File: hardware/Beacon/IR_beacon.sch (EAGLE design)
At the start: 10 parts

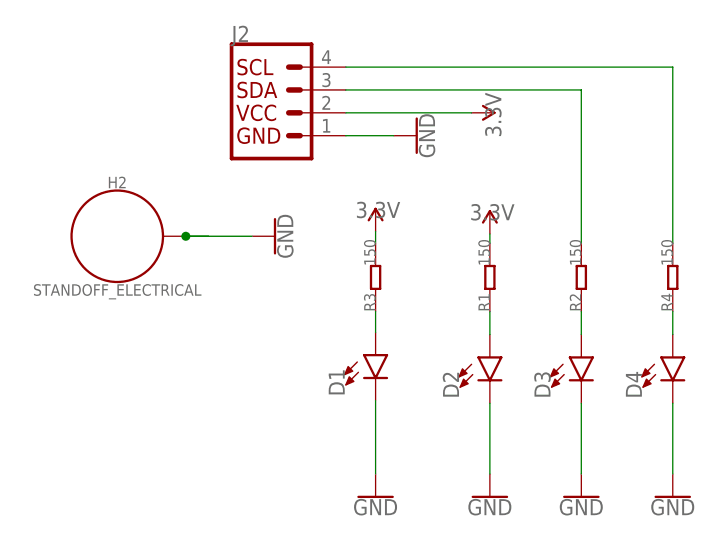
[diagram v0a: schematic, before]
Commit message: Finished Cad files for beacon, and added new 5 bit patern for markers.
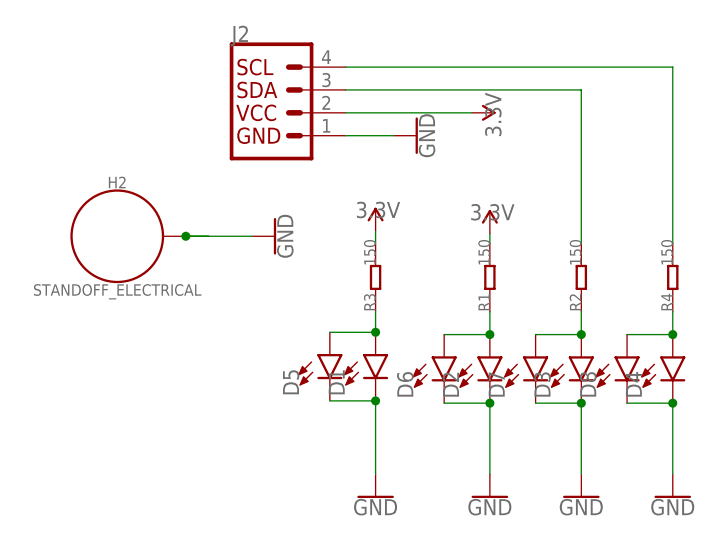
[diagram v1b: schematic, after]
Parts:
- added D5, D6, D7, D8: (no value), SparkFun-LED:LED-FKIT-1206
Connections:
- net GND: now also D5.C, D6.C, D7.C, D8.C
- net N$2: now also D5.A
- net N$3: now also D7.A
- net N$4: now also D6.A
- net N$5: now also D8.A
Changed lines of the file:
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@@
 <?xml version="1.0" encoding="utf-8"?>
 <!DOCTYPE eagle SYSTEM "eagle.dtd">
-<eagle version="9.2.2">
+<eagle version="9.4.2">
 <drawing>
 <settings>
@@
 <part name="J2" library="IAD-Library" deviceset="QWIIC_CONNECTOR" device="JS-1MM"/>
 <part name="H2" library="IAD-Library" deviceset="STANDOFF_ELECTRICAL" device=""/>
+<part name="D5" library="SparkFun-LED" deviceset="LED" device="-FKIT-1206"/>
+<part name="D6" library="SparkFun-LED" deviceset="LED" device="-FKIT-1206"/>
+<part name="D7" library="SparkFun-LED" deviceset="LED" device="-FKIT-1206"/>
+<part name="D8" library="SparkFun-LED" deviceset="LED" device="-FKIT-1206"/>
 </parts>
 <sheets>
@@
 <attribute name="VALUE" x="149.86" y="65.786" size="1.27" layer="96" font="vector" rot="R180" align="bottom-center"/>
 </instance>
+<instance part="D5" gate="G$1" x="173.482" y="57.912" smashed="yes">
+<attribute name="NAME" x="170.053" y="53.34" size="1.778" layer="95" font="vector" rot="R90"/>
+<attribute name="VALUE" x="175.387" y="53.34" size="1.778" layer="96" font="vector" rot="R90" align="top-left"/>
+</instance>
+<instance part="D6" gate="G$1" x="186.182" y="57.658" smashed="yes">
+<attribute name="NAME" x="182.753" y="53.086" size="1.778" layer="95" font="vector" rot="R90"/>
+<attribute name="VALUE" x="188.087" y="53.086" size="1.778" layer="96" font="vector" rot="R90" align="top-left"/>
+</instance>
+<instance part="D7" gate="G$1" x="196.342" y="57.658" smashed="yes">
+<attribute name="NAME" x="192.913" y="53.086" size="1.778" layer="95" font="vector" rot="R90"/>
+<attribute name="VALUE" x="198.247" y="53.086" size="1.778" layer="96" font="vector" rot="R90" align="top-left"/>
+</instance>
+<instance part="D8" gate="G$1" x="206.502" y="57.658" smashed="yes">
+<attribute name="NAME" x="203.073" y="53.086" size="1.778" layer="95" font="vector" rot="R90"/>
+<attribute name="VALUE" x="208.407" y="53.086" size="1.778" layer="96" font="vector" rot="R90" align="top-left"/>
+</instance>
 </instances>
 <busses>
@@
 <wire x1="178.562" y1="62.738" x2="178.562" y2="60.452" width="0.1524" layer="91"/>
 <pinref part="D1" gate="G$1" pin="A"/>
+<pinref part="D5" gate="G$1" pin="A"/>
+<wire x1="178.562" y1="60.452" x2="173.482" y2="60.452" width="0.1524" layer="91"/>
+<junction x="178.562" y="60.452"/>
 </segment>
 </net>
@@
 <wire x1="191.262" y1="62.738" x2="191.262" y2="60.198" width="0.1524" layer="91"/>
 <pinref part="D2" gate="G$1" pin="A"/>
+<pinref part="D6" gate="G$1" pin="A"/>
+<wire x1="191.262" y1="60.198" x2="186.182" y2="60.198" width="0.1524" layer="91"/>
+<junction x="191.262" y="60.198"/>
 </segment>
 </net>
@@
 <wire x1="201.422" y1="62.738" x2="201.422" y2="60.198" width="0.1524" layer="91"/>
 <pinref part="D3" gate="G$1" pin="A"/>
+<pinref part="D7" gate="G$1" pin="A"/>
+<wire x1="201.422" y1="60.198" x2="196.342" y2="60.198" width="0.1524" layer="91"/>
+<junction x="201.422" y="60.198"/>
 </segment>
 </net>
@@
 <wire x1="211.582" y1="62.738" x2="211.582" y2="60.198" width="0.1524" layer="91"/>
 <pinref part="D4" gate="G$1" pin="A"/>
+<pinref part="D8" gate="G$1" pin="A"/>
+<wire x1="206.502" y1="60.198" x2="211.582" y2="60.198" width="0.1524" layer="91"/>
+<junction x="211.582" y="60.198"/>
 </segment>
 </net>
@@
 <wire x1="178.562" y1="52.832" x2="178.562" y2="44.704" width="0.1524" layer="91"/>
 <pinref part="D1" gate="G$1" pin="C"/>
+<pinref part="D5" gate="G$1" pin="C"/>
+<wire x1="178.562" y1="52.832" x2="173.482" y2="52.832" width="0.1524" layer="91"/>
+<junction x="178.562" y="52.832"/>
 </segment>
 <segment>
@@
 <wire x1="191.262" y1="52.578" x2="191.262" y2="44.704" width="0.1524" layer="91"/>
 <pinref part="D2" gate="G$1" pin="C"/>
+<pinref part="D6" gate="G$1" pin="C"/>
+<wire x1="186.182" y1="52.578" x2="191.262" y2="52.578" width="0.1524" layer="91"/>
+<junction x="191.262" y="52.578"/>
 </segment>
 <segment>
@@
 <wire x1="201.422" y1="52.578" x2="201.422" y2="44.704" width="0.1524" layer="91"/>
 <pinref part="D3" gate="G$1" pin="C"/>
+<pinref part="D7" gate="G$1" pin="C"/>
+<wire x1="196.342" y1="52.578" x2="201.422" y2="52.578" width="0.1524" layer="91"/>
+<junction x="201.422" y="52.578"/>
 </segment>
 <segment>
@@
 <wire x1="211.582" y1="52.578" x2="211.582" y2="44.704" width="0.1524" layer="91"/>
 <pinref part="D4" gate="G$1" pin="C"/>
-</segment>
-<segment>
+<pinref part="D8" gate="G$1" pin="C"/>
+<wire x1="211.582" y1="52.578" x2="206.502" y2="52.578" width="0.1524" layer="91"/>
+<junction x="211.582" y="52.578"/>
+</segment>
+<segment>
